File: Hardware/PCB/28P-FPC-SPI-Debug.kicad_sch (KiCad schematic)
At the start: 35 parts, among them J1 Conn_01x08, J2 Conn_01x24, J3 SFV24R-1STBE1HLF, Q1 Si1308EDL, Q2 AO3401A, Q3 S8050, U1 RT9193-33GB, U2 TXB0108PW

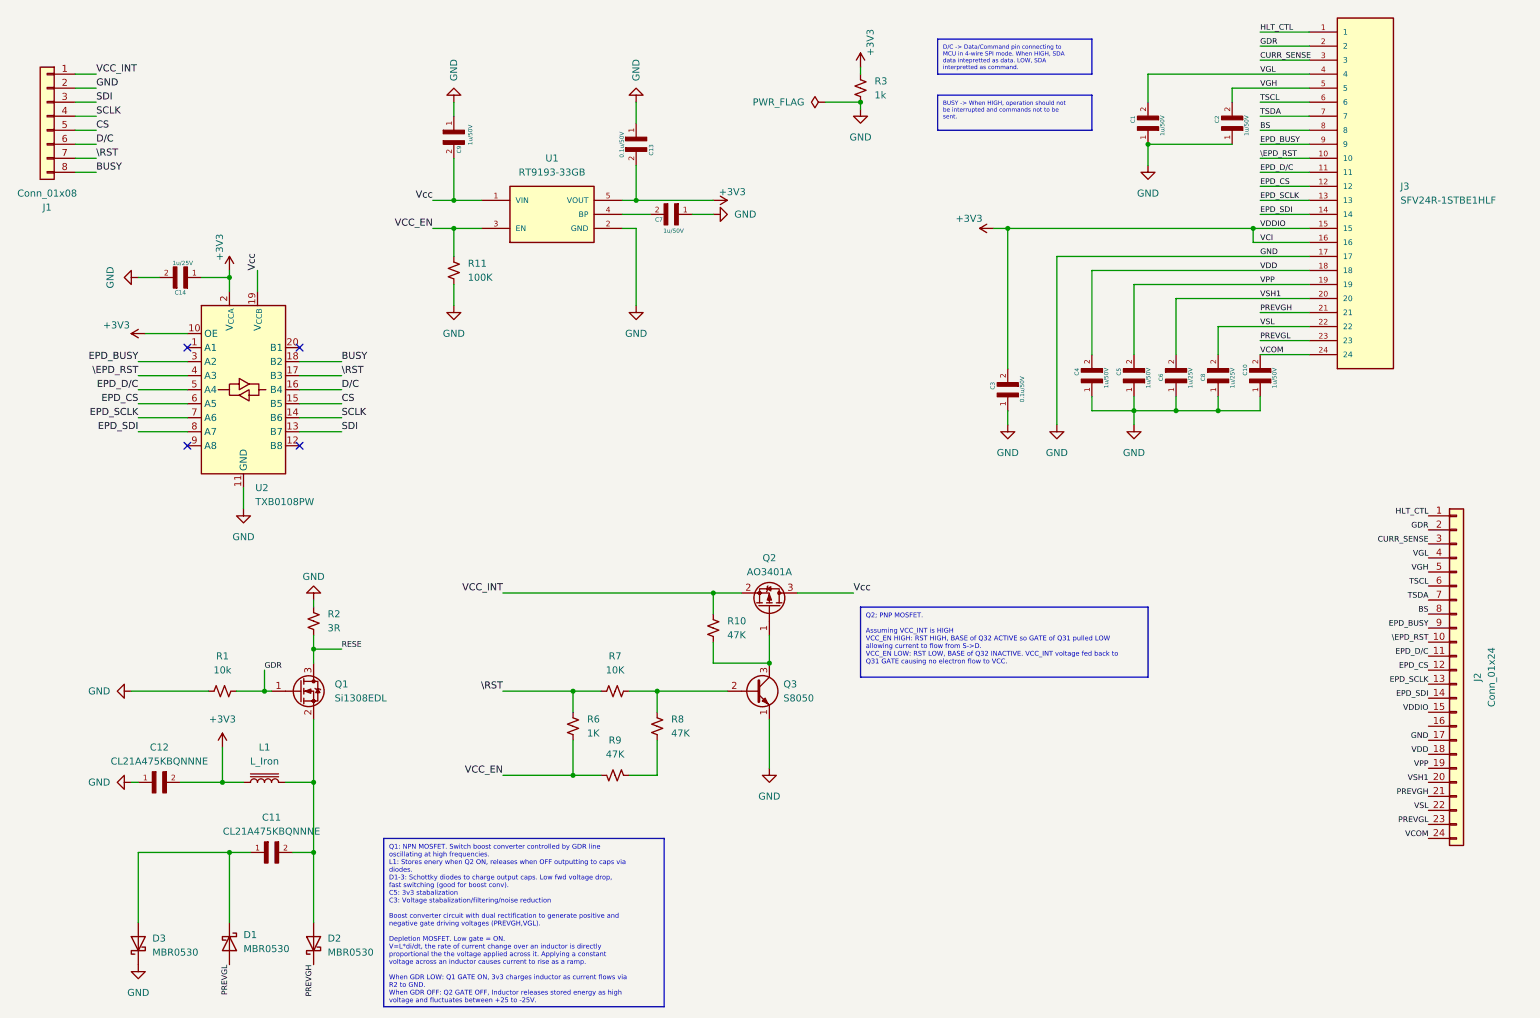
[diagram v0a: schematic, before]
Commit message: Modified J1 footprint to 1.7mm through hole. Added copper pours and GND via stitching for thermal relief. Plus some other stuff I can't remember. E-paper waveshare libs added to STM32 project. Project configuration via MXCube, pin assignment, clock configuration. Basic framework setup for testing.
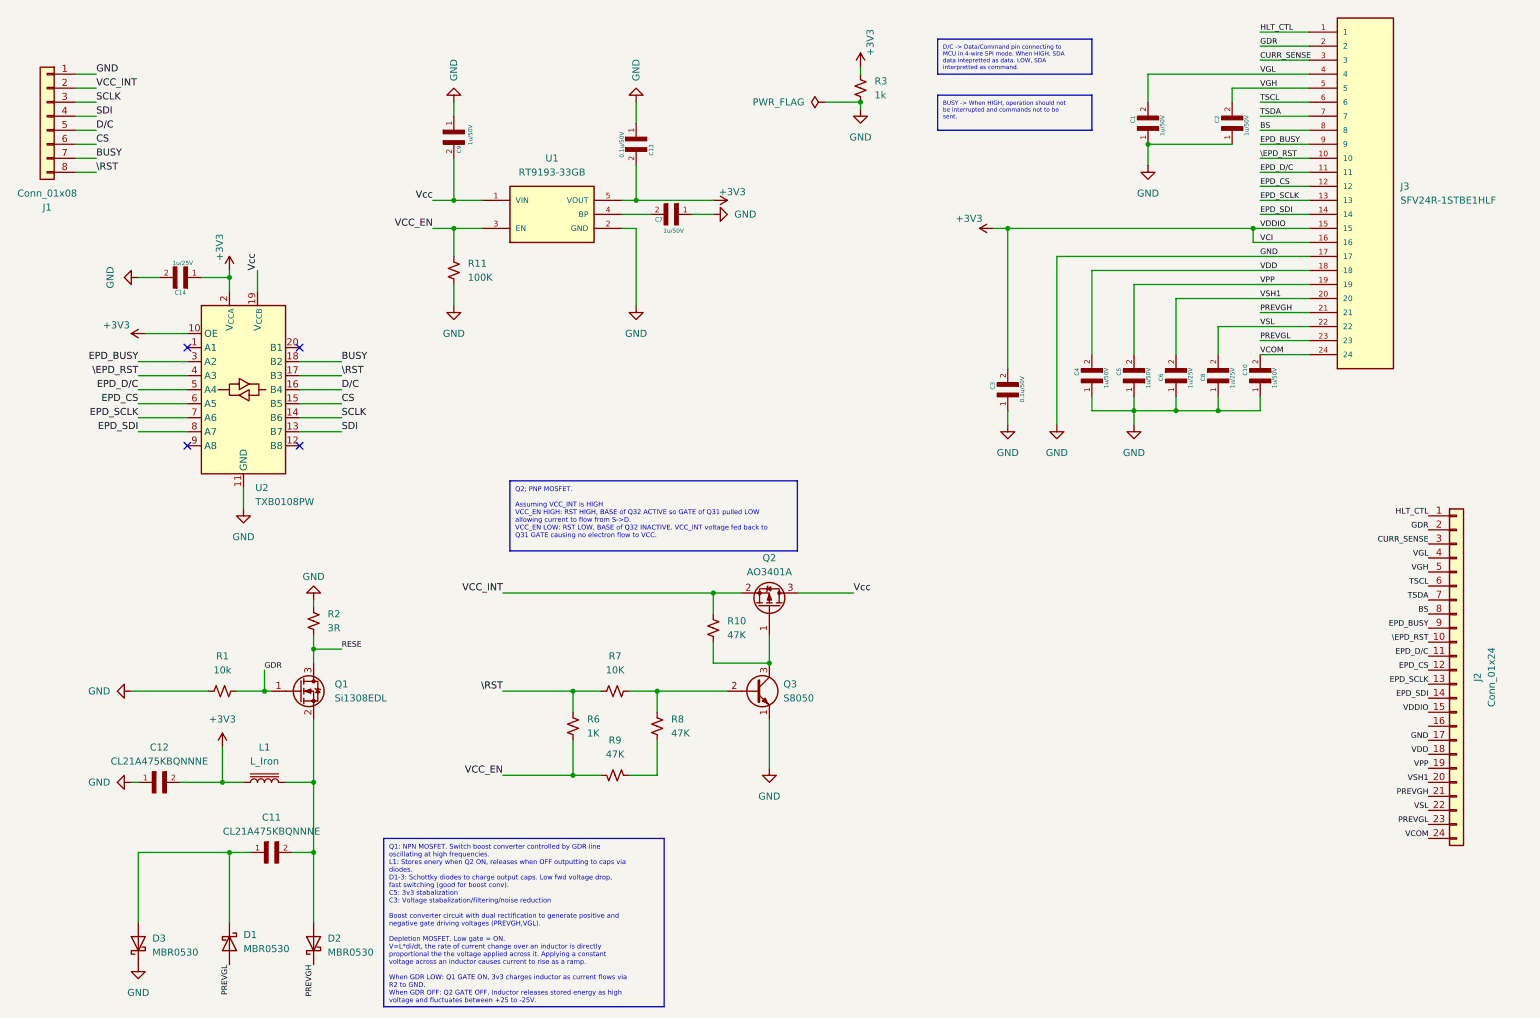
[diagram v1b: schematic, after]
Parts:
- J1: footprint Connector_Samtec_HLE_THT:Samtec_HLE-104-02-xx-DV-TE_2x04_P2.54mm_Horizontal -> Connector_PinHeader_2.54mm:PinHeader_2x04_P2.54mm_Vertical
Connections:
- net BUSY: now also J1.7 (Pin_7); no longer J1.8 (Pin_8)
- net CS: now also J1.6 (Pin_6); no longer J1.5 (Pin_5)
- net D/C: now also J1.5 (Pin_5); no longer J1.6 (Pin_6)
- net GND: now also J1.1 (Pin_1); no longer J1.2 (Pin_2)
- net SCLK: now also J1.3 (Pin_3); no longer J1.4 (Pin_4)
- net SDI: now also J1.4 (Pin_4); no longer J1.3 (Pin_3)
- net VCC_INT: now also J1.2 (Pin_2); no longer J1.1 (Pin_1)
- net \RST: now also J1.8 (Pin_8); no longer J1.7 (Pin_7)
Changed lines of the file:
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@@
 	(text_box "Q2; PNP MOSFET.\n\nAssuming VCC_INT is HIGH\nVCC_EN HIGH: RST HIGH, BASE of Q32 ACTIVE so GATE of Q31 pulled LOW allowing current to flow from S->D.\nVCC_EN LOW: RST LOW, BASE of Q32 INACTIVE. VCC_INT voltage fed back to Q31 GATE causing no electron flow to VCC."
 		(exclude_from_sim no)
-		(at 166.37 120.65 0)
+		(at 102.87 97.79 0)
 		(size 52.07 12.7)
 		(margins 0.9525 0.9525 0.9525 0.9525)
@@
 		)
 	)
-	(label "GND"
-		(at 27.94 26.67 0)
+	(label "SCLK"
+		(at 27.94 29.21 0)
 		(effects
 			(font
@@
 		)
 	)
-	(label "CS"
+	(label "D{slash}C"
 		(at 27.94 34.29 0)
 		(effects
@@
 		)
 	)
-	(label "VSL"
-		(at 269.24 157.48 180)
+	(label "GND"
+		(at 27.94 24.13 0)
 		(effects
 			(font
-				(size 1.016 1.016)
+				(size 1.27 1.27)
 			)
-			(justify right bottom)
+			(justify left bottom)
 		)
 	)
-	(label "CURR_SENSE"
-		(at 269.24 109.22 180)
+	(label "VCC_INT"
+		(at 27.94 26.67 0)
 		(effects
 			(font
-				(size 1.016 1.016)
+				(size 1.27 1.27)
 			)
-			(justify right bottom)
+			(justify left bottom)
 		)
 	)
-	(label "SCLK"
-		(at 27.94 31.75 0)
+	(label "VSL"
+		(at 269.24 157.48 180)
 		(effects
 			(font
-				(size 1.27 1.27)
+				(size 1.016 1.016)
 			)
-			(justify left bottom)
+			(justify right bottom)
 		)
 	)
-	(label "VCC_INT"
-		(at 101.6 118.11 180)
+	(label "CURR_SENSE"
+		(at 269.24 109.22 180)
 		(effects
 			(font
-				(size 1.27 1.27)
+				(size 1.016 1.016)
 			)
 			(justify right bottom)
 		)
 	)
-	(label "D{slash}C"
-		(at 27.94 36.83 0)
+	(label "BUSY"
+		(at 27.94 39.37 0)
 		(effects
 			(font
@@
 		)
 	)
-	(label "SDI"
-		(at 27.94 29.21 0)
+	(label "VCC_INT"
+		(at 101.6 118.11 180)
 		(effects
 			(font
 				(size 1.27 1.27)
 			)
-			(justify left bottom)
+			(justify right bottom)
 		)
 	)
@@
 		)
 	)
+	(label "SDI"
+		(at 27.94 31.75 0)
+		(effects
+			(font
+				(size 1.27 1.27)
+			)
+			(justify left bottom)
+		)
+	)
 	(label "VPP"
 		(at 238.76 62.23 0)
@@
 		)
 	)
-	(label "VCC_INT"
-		(at 27.94 24.13 0)
+	(label "VGH"
+		(at 238.76 26.67 0)
 		(effects
 			(font
-				(size 1.27 1.27)
+				(size 1.016 1.016)
 			)
 			(justify left bottom)
 		)
 	)
-	(label "VGH"
-		(at 238.76 26.67 0)
+	(label "CS"
+		(at 72.39 83.82 0)
 		(effects
 			(font
-				(size 1.016 1.016)
+				(size 1.27 1.27)
 			)
 			(justify left bottom)
 		)
 	)
-	(label "CS"
-		(at 72.39 83.82 0)
+	(label "\\RST"
+		(at 27.94 41.91 0)
 		(effects
 			(font
@@
 		)
 	)
-	(label "\\RST"
-		(at 27.94 39.37 0)
-		(effects
-			(font
-				(size 1.27 1.27)
-			)
-			(justify left bottom)
-		)
-	)
 	(label "D{slash}C"
 		(at 72.39 81.28 0)
@@
 		)
 	)
+	(label "CS"
+		(at 27.94 36.83 0)
+		(effects
+			(font
+				(size 1.27 1.27)
+			)
+			(justify left bottom)
+		)
+	)
 	(label "EPD_CS"
 		(at 35.56 83.82 180)
@@
 		)
 	)
-	(label "BUSY"
-		(at 27.94 41.91 0)
-		(effects
-			(font
-				(size 1.27 1.27)
-			)
-			(justify left bottom)
-		)
-	)
 	(label "VPP"
 		(at 269.24 149.86 180)
@@
 			)
 		)
-		(property "Footprint" "Connector_Samtec_HLE_THT:Samtec_HLE-104-02-xx-DV-TE_2x04_P2.54mm_Horizontal"
+		(property "Footprint" "Connector_PinHeader_2.54mm:PinHeader_2x04_P2.54mm_Vertical"
 			(at 19.05 31.75 0)
 			(effects

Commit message: Mirror pins on FPC connector. Reposition components. Copper pours
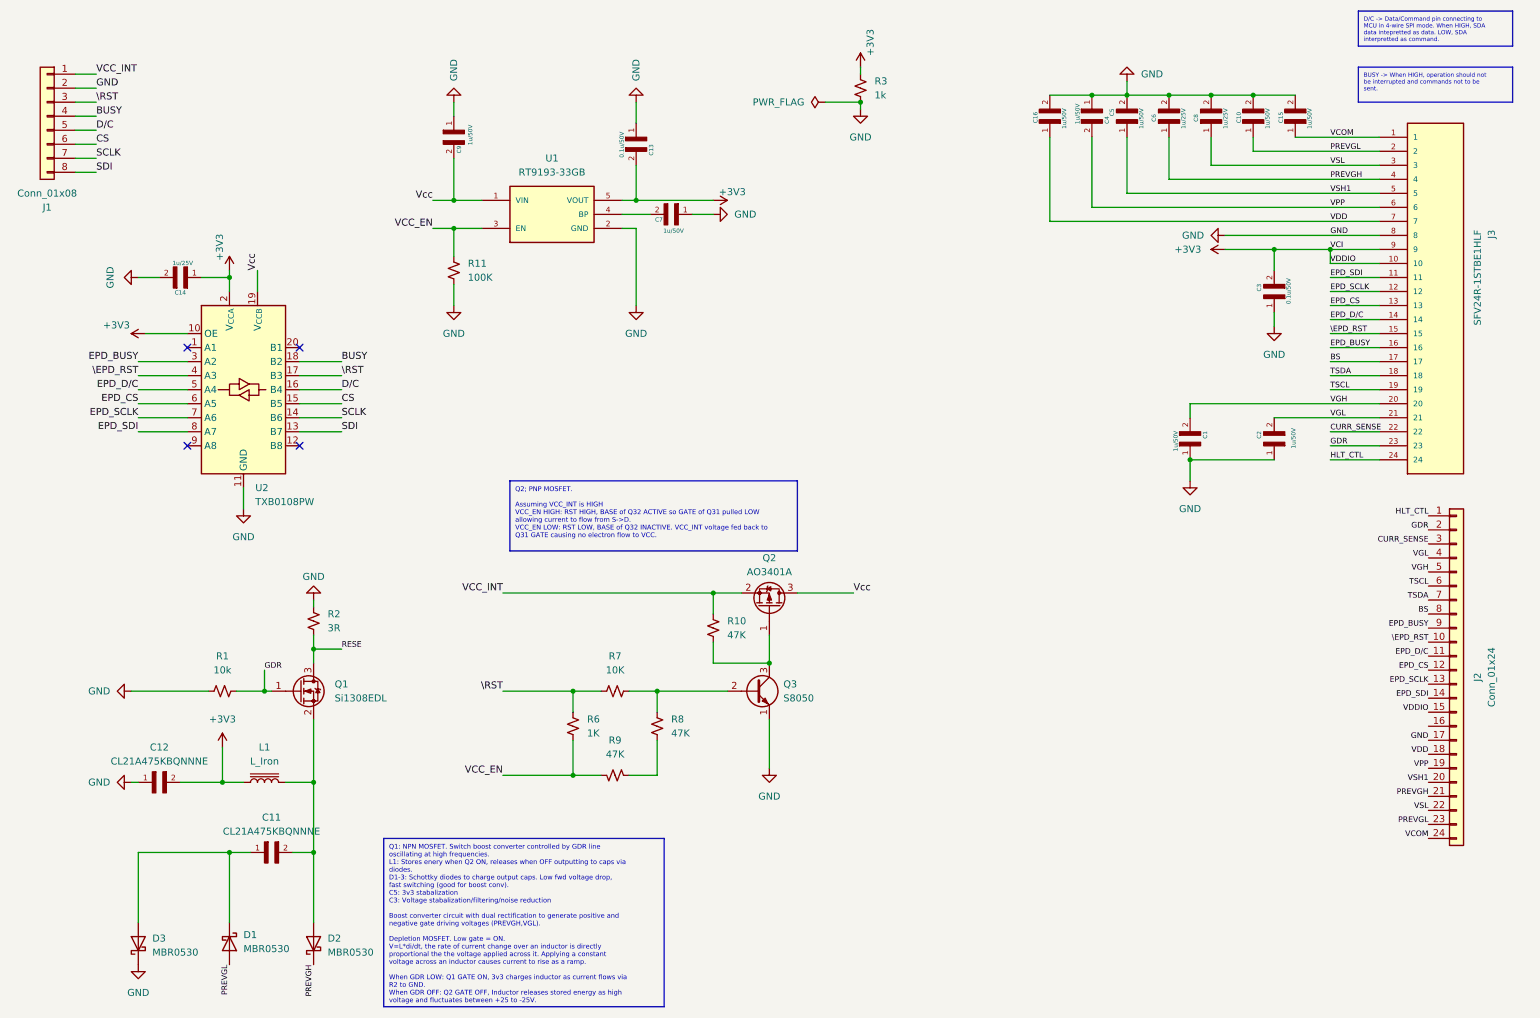
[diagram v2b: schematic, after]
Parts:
- added C15, C16: 1u/50V, capacitors-cam:CAPC2012X140N, symbol Capacitors:MBASU168AB5105KTNA01
- J1: footprint Connector_PinHeader_2.54mm:PinHeader_2x04_P2.54mm_Vertical -> Connector_PinHeader_2.54mm:PinHeader_1x08_P2.54mm_Vertical
- J2: footprint Connector_PinHeader_2.54mm:PinHeader_2x12_P2.54mm_Vertical -> Connector_PinHeader_2.54mm:PinHeader_2x12_P2.54mm_Vertical_SMD
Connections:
- net +3V3: now also J3.10, J3.9; no longer J3.15, J3.16
- net BS: now also J3.17; no longer J3.8
- net BUSY: now also J1.4 (Pin_4); no longer J1.7 (Pin_7)
- net CURR_SENSE: now also J3.22; no longer J3.3
- net EPD_BUSY: now also J3.16; no longer J3.9
- net EPD_CS: now also J3.13; no longer J3.12
- net EPD_D/C: now also J3.14; no longer J3.11
- net EPD_SCLK: now also J3.12; no longer J3.13
- net EPD_SDI: now also J3.11; no longer J3.14
- net GDR: now also J3.23; no longer J3.2
- net GND: now also C10.2, C5.2, C6.2, C8.2, J1.2 (Pin_2), J3.8, C15.2, C16.2; no longer C10.1, C5.1, C6.1, C8.1, J1.1 (Pin_1), J3.17
- net HLT_CTL: now also J3.24; no longer J3.1
- net PREVGH: now also C6.1, J3.4; no longer J3.21
- net PREVGL: now also C10.1, J3.2; no longer J3.23
- net SCLK: now also J1.7 (Pin_7); no longer J1.3 (Pin_3)
- net SDI: now also J1.8 (Pin_8); no longer J1.4 (Pin_4)
- net TSCL: now also J3.19; no longer J3.6
- net TSDA: now also J3.18; no longer J3.7
- net VCC_INT: now also J1.1 (Pin_1); no longer J1.2 (Pin_2)
- net VCOM: now also J3.1, C15.1; no longer C10.2, J3.24
- net VDD: now also J3.7, C16.1; no longer C4.2, J3.18
- net VGH: now also C1.2, J3.20; no longer C2.2, J3.5
- net VGL: now also C2.2, J3.21; no longer C1.2, J3.4
- net VPP: now also C4.2, J3.6; no longer C5.2, J3.19
- net VSH1: now also C5.1, J3.5; no longer C6.2, J3.20
- net VSL: now also C8.1, J3.3; no longer C8.2, J3.22
- net \EPD_RST: now also J3.15; no longer J3.10
- net \RST: now also J1.3 (Pin_3); no longer J1.8 (Pin_8)
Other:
- moved on the sheet: C1, C10, C2, C3, C4, C5, C6, C8, J3

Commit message: Modified J3 FPC connector to top bottom connector FFC2B28-24-G.
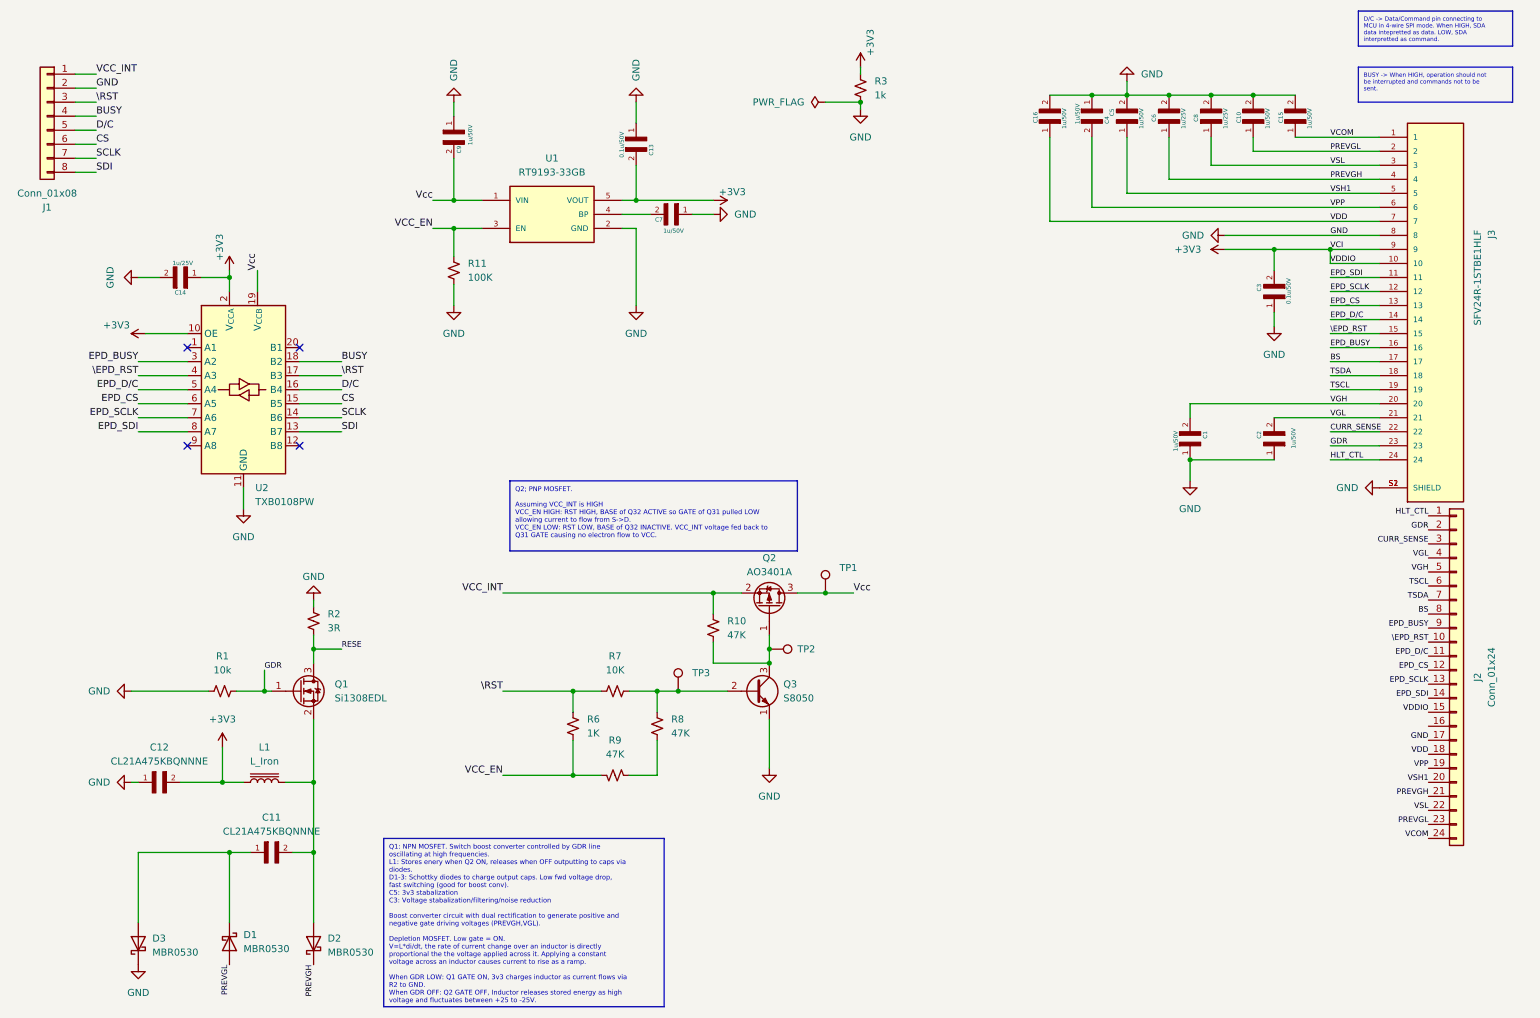
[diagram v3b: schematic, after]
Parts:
- added TP1, TP2, TP3: ~, TestPoint:TestPoint_THTPad_1.0x1.0mm_Drill0.5mm, symbol Connector:TestPoint
- J3: footprint Connectors-cam:AMPHENOL_SFV24R-1STBE1HLF -> FFC2B28-24-G:GCT_FFC2B28-24-G; symbol Connector_FFC-FPC:SFV24R-1STBE1HLF -> connector-lib:FFC2B28-24-G; Availability (none) -> In Stock; Check_prices (none) -> https://www.snapeda.com/parts/FFC2B28-24-G/Global+Connector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; Description_1 (none) -> 24 Position FFC, FPC Connector Contacts, Top and Bottom 0.0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; MANUFACTURER Amphenol -> GCT; MAXIMUM_PACKAGE_HEIGHT 2.36mm -> 1.75mm; MF (none) -> Global Connector Technology; MP (none) -> FFC2B28-24-G; PARTREV B -> A; Package (none) -> None; Price (none) -> None; SnapEDA_Link (none) -> https://www.snapeda.com/parts/FFC2B28-24-G/Global+Connector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
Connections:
- net GND: now also J3.S1 (SHIELD), J3.S2 (SHIELD)
- net Vcc: now also TP1.1
- net at Q2.1 (G), Q3.3 (C), R10.1: now also TP2.1
- net at Q3.2 (B), R7.1, R8.2: now also TP3.1
